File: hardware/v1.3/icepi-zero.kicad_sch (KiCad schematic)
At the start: 29 parts, among them J1 Conn_02x20_Counter_Clockwise, SW1 SW_Push, SW2 SW_Push, U1 ECP5-CABGA256, Y1 SG-8018CG 50.000000MHz

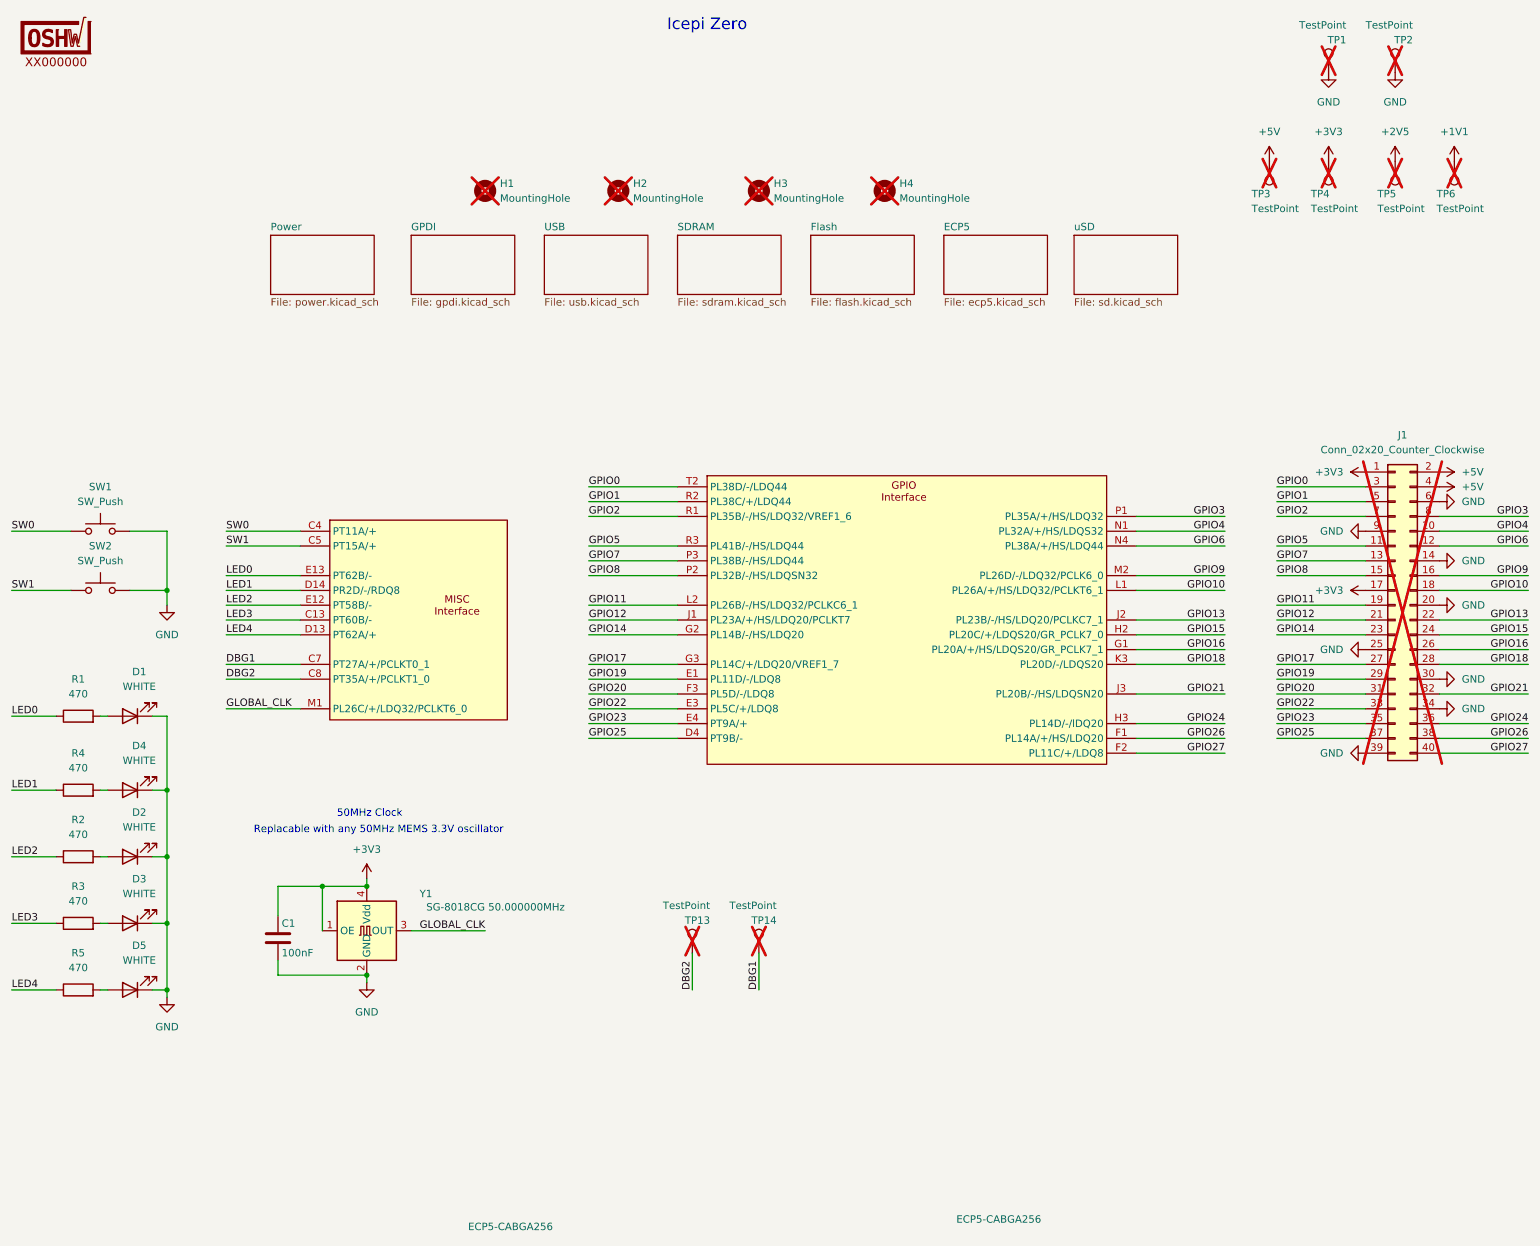
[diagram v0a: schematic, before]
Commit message: Refine README
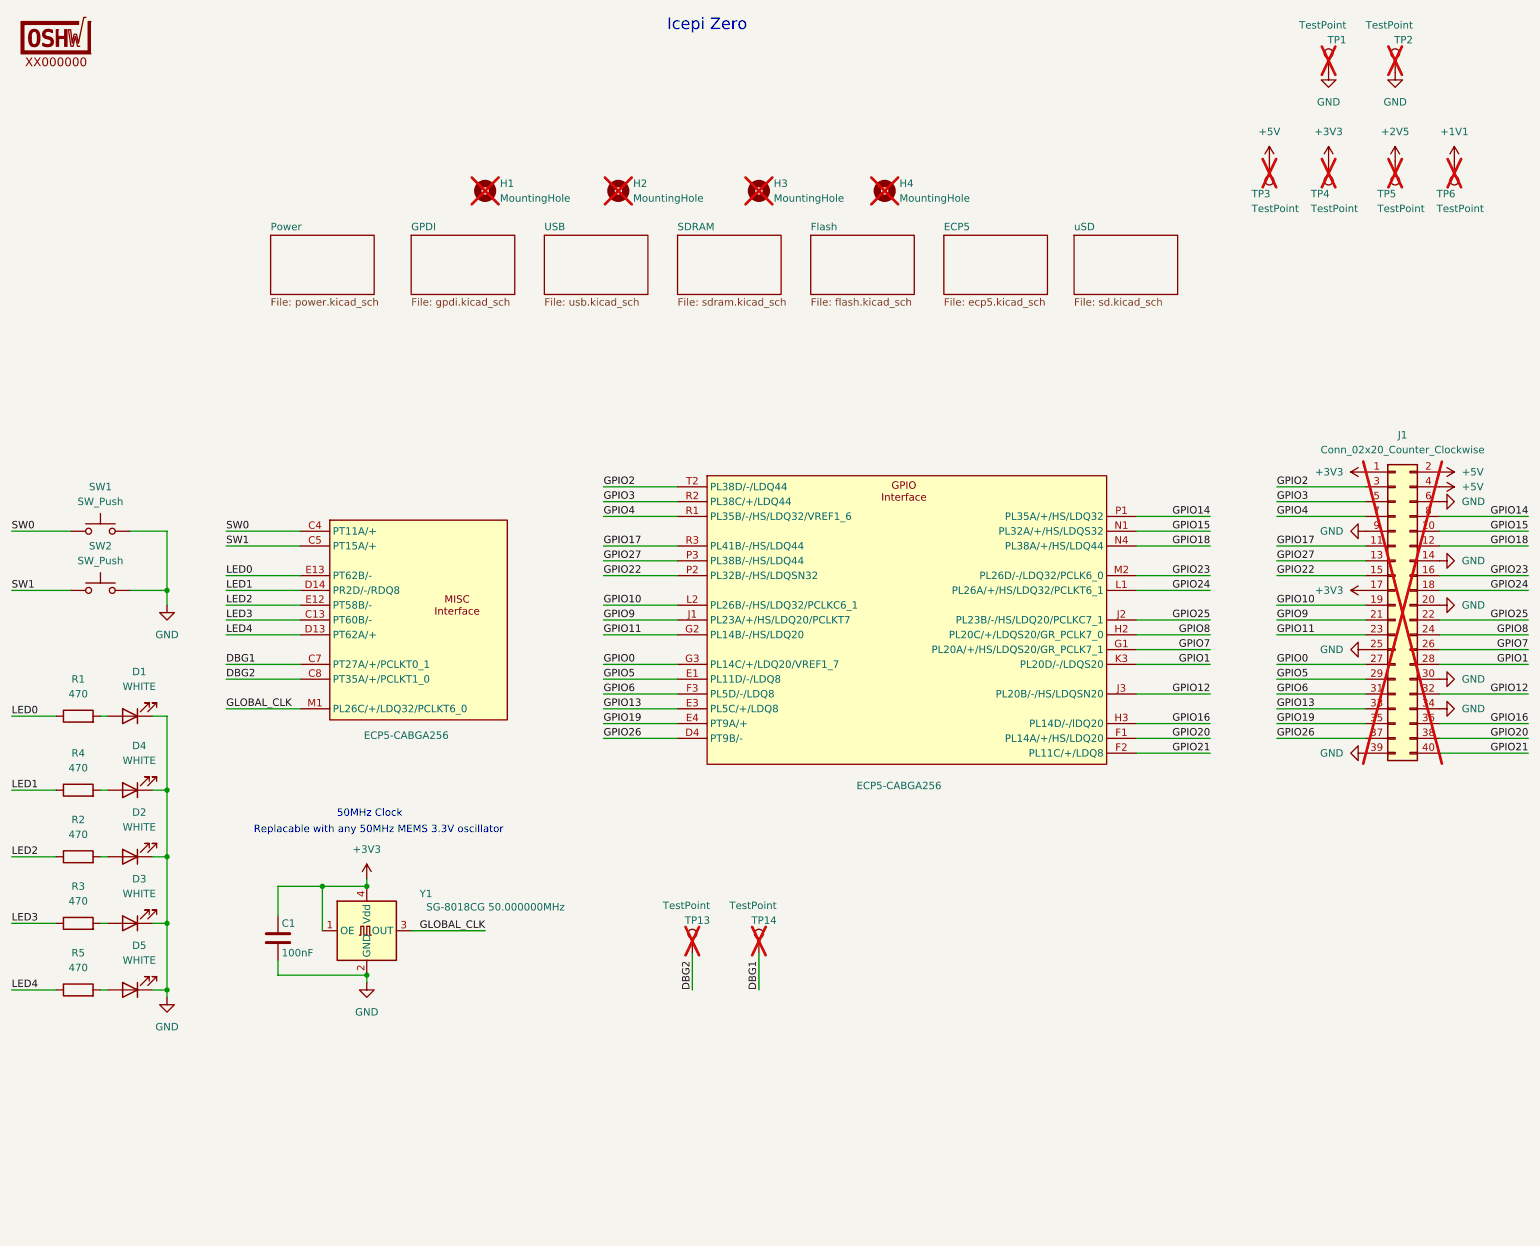
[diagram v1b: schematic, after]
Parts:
- C1: LCSC Link (none) -> https://lcsc.com/product-detail/Multilayer-Ceramic-Capacito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; LCSC Part # C307331 -> C307331; Manufactuer Part Number (none) -> CL05B104KB54PNC
- D1, D2, D3, D4, D5: LCSC Link (none) -> https://lcsc.com/product-detail/LED-Indication-Discrete_Hub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; Manufactuer Part Number (none) -> KT-0603W
- R1, R2, R3, R4, R5: LCSC Link (none) -> https://lcsc.com/product-detail/Chip-Resistor-Surface-Mount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; Manufactuer Part Number (none) -> 0402WGF4700TCE
- SW1, SW2: LCSC Link (none) -> https://lcsc.com/product-detail/Tactile-Switches_XUNPU-TS-1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; Manufactuer Part Number (none) -> TS-1088-AR02016
- U1: LCSC Link (none) -> https://lcsc.com/product-detail/Programmable-Logic-Device-C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; LCSC Part # (none) -> C1521614; Manufactuer Part Number (none) -> LFE5U-25F-6BG256C
- Y1: LCSC Link (none) -> https://lcsc.com/product-detail/Programmable-Oscillators_EP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; Manufactuer Part Number (none) -> SG-8018CG 50.000000MHz TJHSA
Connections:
- net GPIO0: now also J1.27 (Pin_27), U1.G3 (PL14C/+/LDQ20/VREF1_7); no longer J1.3 (Pin_3), U1.T2 (PL38D/-/LDQ44)
- net GPIO1: now also J1.28 (Pin_28), U1.K3 (PL20D/-/LDQS20); no longer J1.5 (Pin_5), U1.R2 (PL38C/+/LDQ44)
- net GPIO10: now also J1.19 (Pin_19), U1.L2 (PL26B/-/HS/LDQ32/PCLKC6_1); no longer J1.18 (Pin_18), U1.L1 (PL26A/+/HS/LDQ32/PCLKT6_1)
- net GPIO11: now also J1.23 (Pin_23), U1.G2 (PL14B/-/HS/LDQ20); no longer J1.19 (Pin_19), U1.L2 (PL26B/-/HS/LDQ32/PCLKC6_1)
- net GPIO12: now also J1.32 (Pin_32), U1.J3 (PL20B/-/HS/LDQSN20); no longer J1.21 (Pin_21), U1.J1 (PL23A/+/HS/LDQ20/PCLKT7)
- net GPIO13: now also J1.33 (Pin_33), U1.E3 (PL5C/+/LDQ8); no longer J1.22 (Pin_22), U1.J2 (PL23B/-/HS/LDQ20/PCLKC7_1)
- net GPIO14: now also J1.8 (Pin_8), U1.P1 (PL35A/+/HS/LDQ32); no longer J1.23 (Pin_23), U1.G2 (PL14B/-/HS/LDQ20)
- net GPIO15: now also J1.10 (Pin_10), U1.N1 (PL32A/+/HS/LDQS32); no longer J1.24 (Pin_24), U1.H2 (PL20C/+/LDQS20/GR_PCLK7_0)
- net GPIO16: now also J1.36 (Pin_36), U1.H3 (PL14D/-/lDQ20); no longer J1.26 (Pin_26), U1.G1 (PL20A/+/HS/LDQS20/GR_PCLK7_1)
- net GPIO17: now also J1.11 (Pin_11), U1.R3 (PL41B/-/HS/LDQ44); no longer J1.27 (Pin_27), U1.G3 (PL14C/+/LDQ20/VREF1_7)
- net GPIO18: now also J1.12 (Pin_12), U1.N4 (PL38A/+/HS/LDQ44); no longer J1.28 (Pin_28), U1.K3 (PL20D/-/LDQS20)
- net GPIO19: now also J1.35 (Pin_35), U1.E4 (PT9A/+); no longer J1.29 (Pin_29), U1.E1 (PL11D/-/LDQ8)
- net GPIO2: now also J1.3 (Pin_3), U1.T2 (PL38D/-/LDQ44); no longer J1.7 (Pin_7), U1.R1 (PL35B/-/HS/LDQ32/VREF1_6)
- net GPIO20: now also J1.38 (Pin_38), U1.F1 (PL14A/+/HS/LDQ20); no longer J1.31 (Pin_31), U1.F3 (PL5D/-/LDQ8)
- net GPIO21: now also J1.40 (Pin_40), U1.F2 (PL11C/+/LDQ8); no longer J1.32 (Pin_32), U1.J3 (PL20B/-/HS/LDQSN20)
- net GPIO22: now also J1.15 (Pin_15), U1.P2 (PL32B/-/HS/LDQSN32); no longer J1.33 (Pin_33), U1.E3 (PL5C/+/LDQ8)
- net GPIO23: now also J1.16 (Pin_16), U1.M2 (PL26D/-/LDQ32/PCLK6_0); no longer J1.35 (Pin_35), U1.E4 (PT9A/+)
- net GPIO24: now also J1.18 (Pin_18), U1.L1 (PL26A/+/HS/LDQ32/PCLKT6_1); no longer J1.36 (Pin_36), U1.H3 (PL14D/-/lDQ20)
- net GPIO25: now also J1.22 (Pin_22), U1.J2 (PL23B/-/HS/LDQ20/PCLKC7_1); no longer J1.37 (Pin_37), U1.D4 (PT9B/-)
- net GPIO26: now also J1.37 (Pin_37), U1.D4 (PT9B/-); no longer J1.38 (Pin_38), U1.F1 (PL14A/+/HS/LDQ20)
- net GPIO27: now also J1.13 (Pin_13), U1.P3 (PL38B/-/HS/LDQ44); no longer J1.40 (Pin_40), U1.F2 (PL11C/+/LDQ8)
- net GPIO3: now also J1.5 (Pin_5), U1.R2 (PL38C/+/LDQ44); no longer J1.8 (Pin_8), U1.P1 (PL35A/+/HS/LDQ32)
- net GPIO4: now also J1.7 (Pin_7), U1.R1 (PL35B/-/HS/LDQ32/VREF1_6); no longer J1.10 (Pin_10), U1.N1 (PL32A/+/HS/LDQS32)
- net GPIO5: now also J1.29 (Pin_29), U1.E1 (PL11D/-/LDQ8); no longer J1.11 (Pin_11), U1.R3 (PL41B/-/HS/LDQ44)
- net GPIO6: now also J1.31 (Pin_31), U1.F3 (PL5D/-/LDQ8); no longer J1.12 (Pin_12), U1.N4 (PL38A/+/HS/LDQ44)
- net GPIO7: now also J1.26 (Pin_26), U1.G1 (PL20A/+/HS/LDQS20/GR_PCLK7_1); no longer J1.13 (Pin_13), U1.P3 (PL38B/-/HS/LDQ44)
- net GPIO8: now also J1.24 (Pin_24), U1.H2 (PL20C/+/LDQS20/GR_PCLK7_0); no longer J1.15 (Pin_15), U1.P2 (PL32B/-/HS/LDQSN32)
- net GPIO9: now also J1.21 (Pin_21), U1.J1 (PL23A/+/HS/LDQ20/PCLKT7); no longer J1.16 (Pin_16), U1.M2 (PL26D/-/LDQ32/PCLK6_0)

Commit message: Update files
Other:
- note added: "Icepi Zero v1.3!"
- note removed: "Icepi Zero"
- moved on the sheet: C1, D1, D2, D3, D4, D5, R1, R2, R3, R4, R5, SW1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

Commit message: Update to v1.3 board
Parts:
- LOGO1: now not fitted
- TP1, TP13, TP14, TP2, TP3, TP4, TP5, TP6: now left out of the parts list

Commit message: Final mass production files
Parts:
- TP1, TP2, TP3, TP4, TP5, TP6: footprint TestPoint:TestPoint_Pad_D2.0mm -> icepi-lib:TestPoint_Pad_D2.0mm_Blank
- TP13, TP14: footprint TestPoint:TestPoint_Pad_D1.0mm -> icepi-lib:TestPoint_Pad_D1.0mm_Blank
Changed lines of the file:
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@@
 			)
 		)
-		(property "Footprint" "TestPoint:TestPoint_Pad_D1.0mm"
+		(property "Footprint" "icepi-lib:TestPoint_Pad_D1.0mm_Blank"
 			(at 149.86 177.8 0)
 			(effects
@@
 			)
 		)
-		(property "Footprint" "TestPoint:TestPoint_Pad_D1.0mm"
+		(property "Footprint" "icepi-lib:TestPoint_Pad_D1.0mm_Blank"
 			(at 138.43 177.8 0)
 			(effects
@@
 			)
 		)
-		(property "Footprint" "TestPoint:TestPoint_Pad_D2.0mm"
+		(property "Footprint" "icepi-lib:TestPoint_Pad_D2.0mm_Blank"
 			(at 227.33 41.91 0)
 			(effects
@@
 			)
 		)
-		(property "Footprint" "TestPoint:TestPoint_Pad_D2.0mm"
+		(property "Footprint" "icepi-lib:TestPoint_Pad_D2.0mm_Blank"
 			(at 259.08 41.91 0)
 			(effects
@@
 			)
 		)
-		(property "Footprint" "TestPoint:TestPoint_Pad_D2.0mm"
+		(property "Footprint" "icepi-lib:TestPoint_Pad_D2.0mm_Blank"
 			(at 259.08 26.67 0)
 			(effects
@@
 			)
 		)
-		(property "Footprint" "TestPoint:TestPoint_Pad_D2.0mm"
+		(property "Footprint" "icepi-lib:TestPoint_Pad_D2.0mm_Blank"
 			(at 247.65 26.67 0)
 			(effects
@@
 			)
 		)
-		(property "Footprint" "TestPoint:TestPoint_Pad_D2.0mm"
+		(property "Footprint" "icepi-lib:TestPoint_Pad_D2.0mm_Blank"
 			(at 248.92 41.91 0)
 			(effects
@@
 			)
 		)
-		(property "Footprint" "TestPoint:TestPoint_Pad_D2.0mm"
+		(property "Footprint" "icepi-lib:TestPoint_Pad_D2.0mm_Blank"
 			(at 237.49 41.91 0)
 			(effects

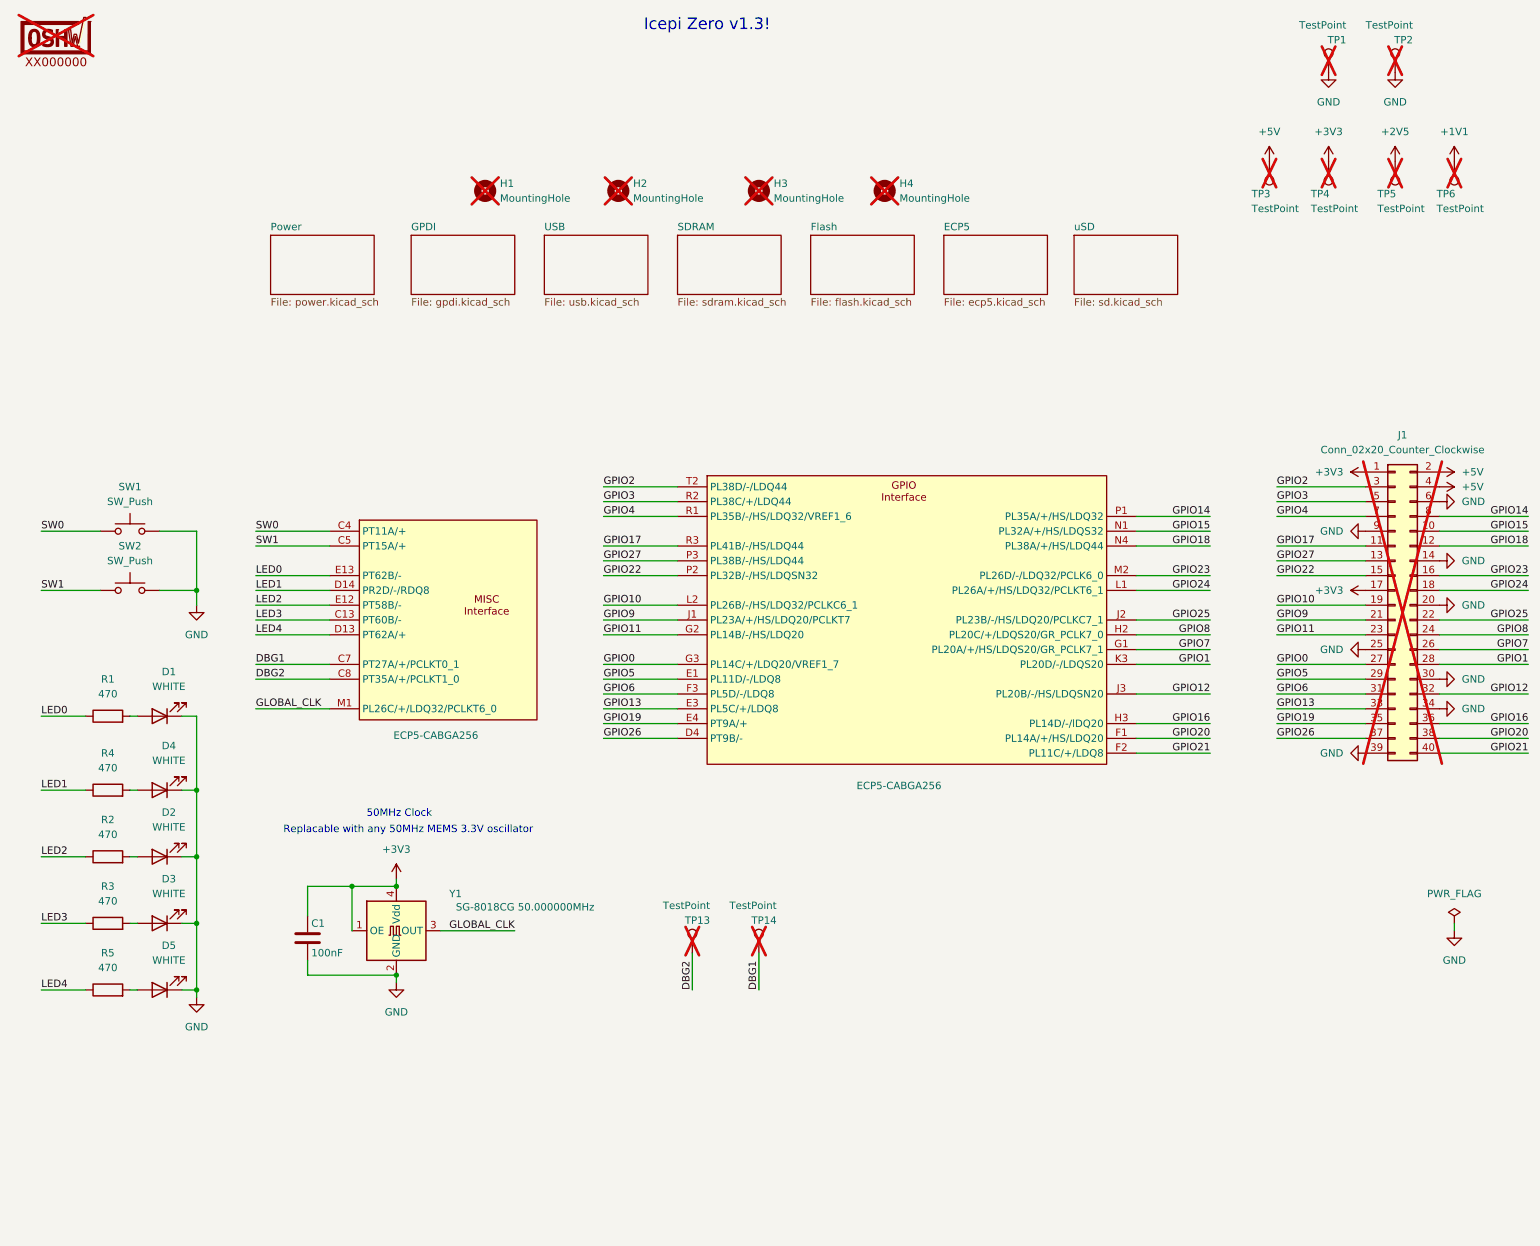
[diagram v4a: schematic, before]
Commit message: Improve makefile and hardware
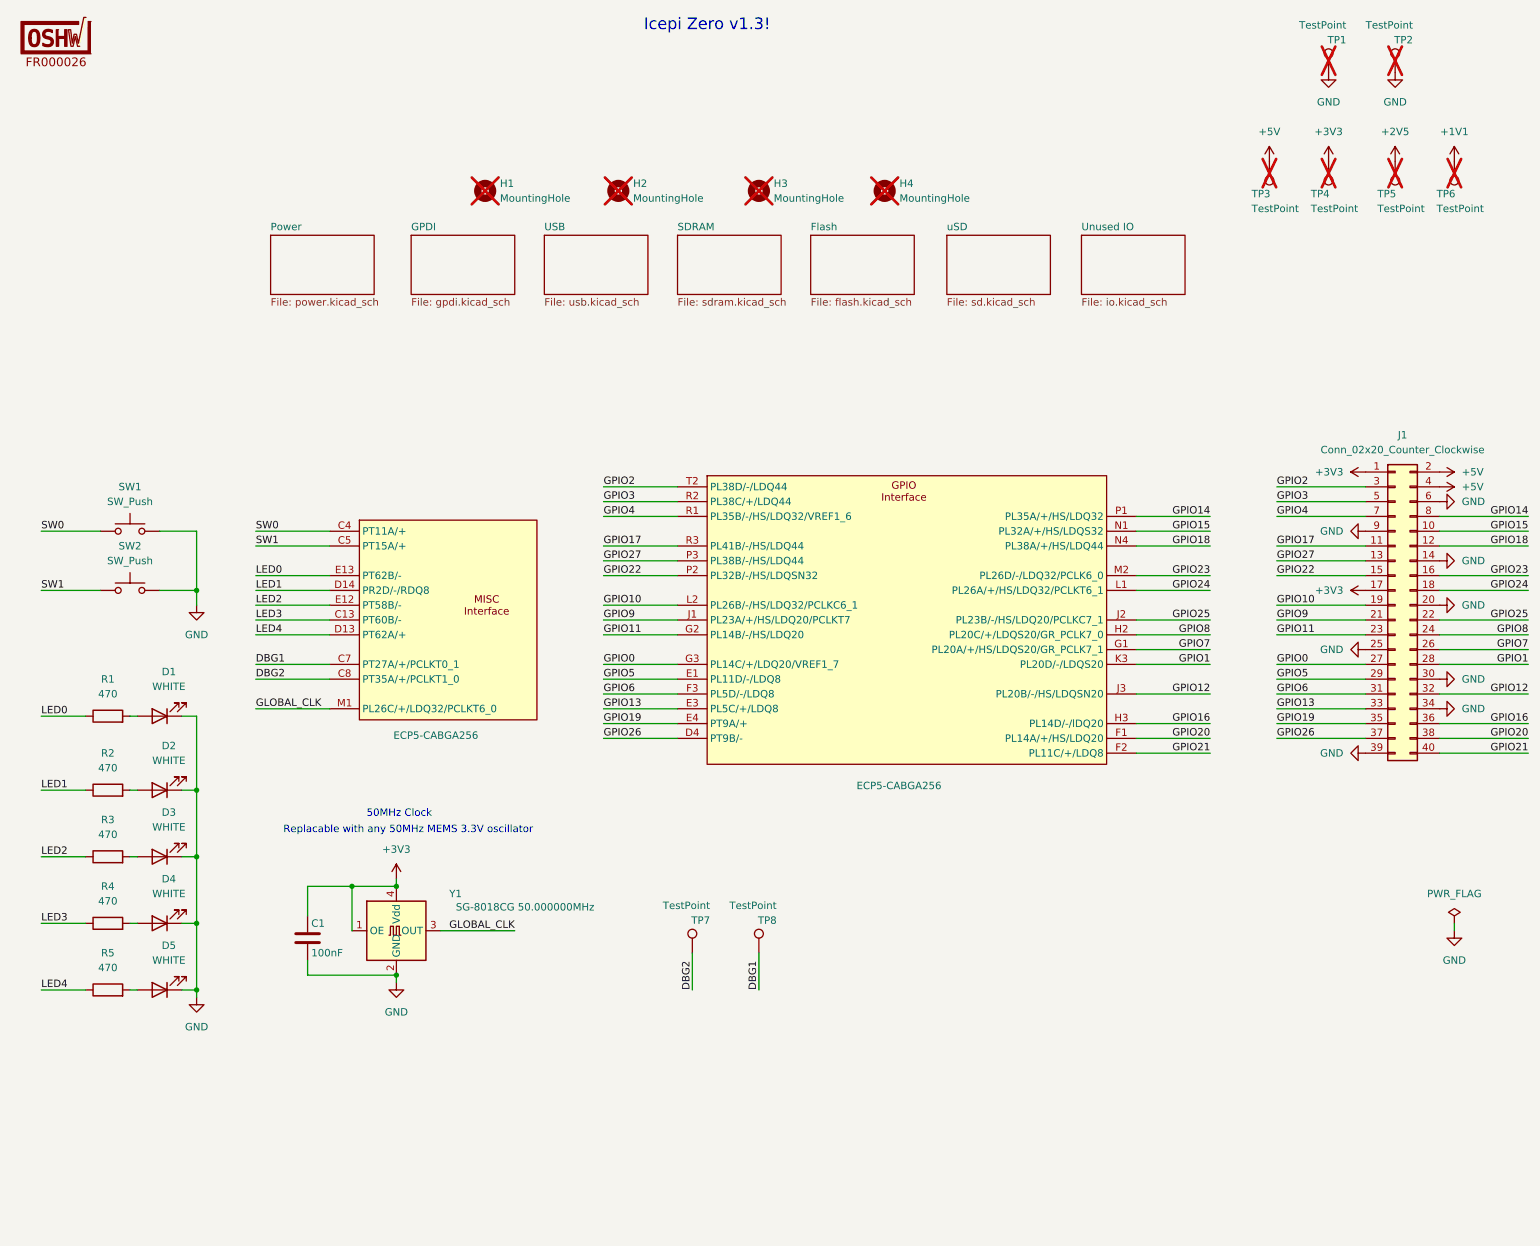
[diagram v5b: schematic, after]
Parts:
- J1, LOGO1: now fitted
- TP7: renamed from TP13; now fitted
- TP8: renamed from TP14; now fitted
- renumbered D4 to D2, D2 to D3, D3 to D4, R4 to R2, R2 to R3, R3 to R4
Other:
- sheet ECP5 renamed Unused IO
- sheet Unused IO: file ecp5.kicad_sch -> io.kicad_sch
- title: Icepi zero -> Icepi Zero
